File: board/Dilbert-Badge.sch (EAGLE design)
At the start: 47 parts, among them IC1 MCP23017SO, J1 IO EXP., J2 FTDI_DEVICE, J3 NEOPIXEL, J4 PWR IN, J5 I2C, SW1 UP, SW2 DOWN, SW3 LEFT, SW4 RIGHT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

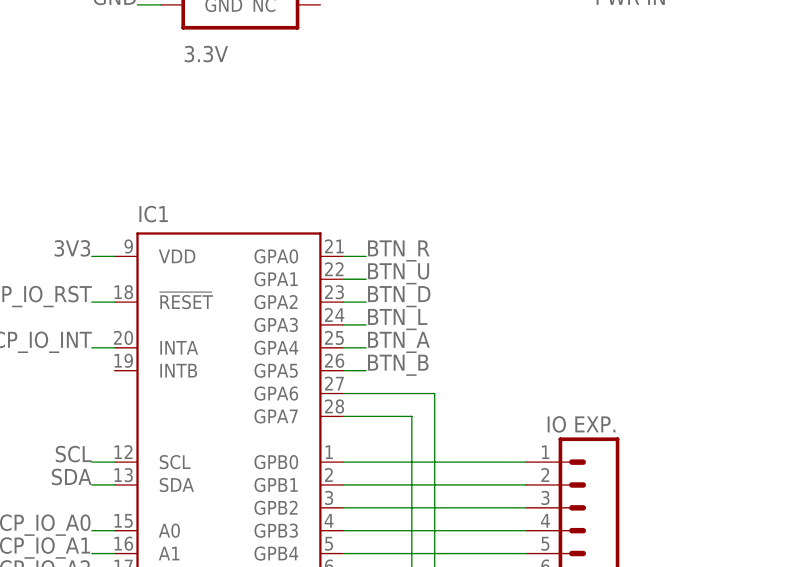
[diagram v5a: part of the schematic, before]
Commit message: swap left/right buttons
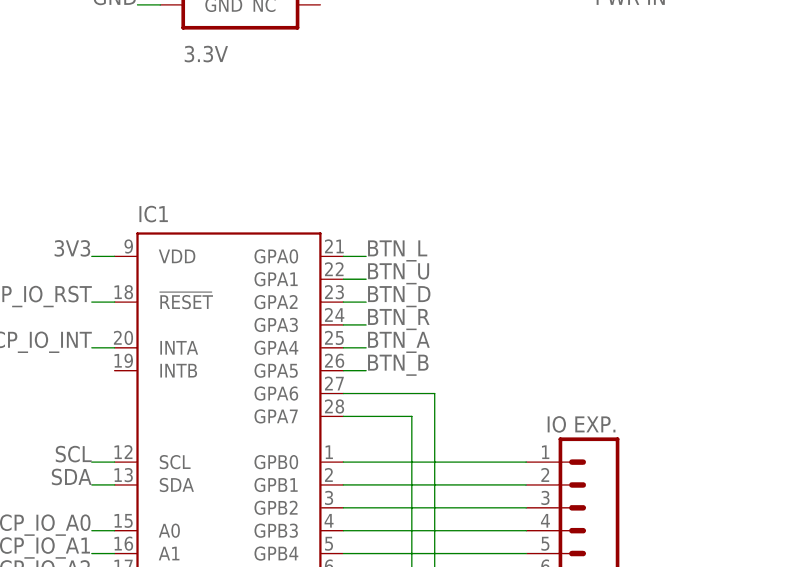
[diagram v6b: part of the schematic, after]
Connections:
- net BTN_L: now also IC1.GPA0; no longer IC1.GPA3
- net BTN_R: now also IC1.GPA3; no longer IC1.GPA0
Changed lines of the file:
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@@
 </segment>
 <segment>
-<pinref part="IC1" gate="G$1" pin="GPA3"/>
-<label x="76.2" y="226.06" size="1.778" layer="95"/>
-<wire x1="76.2" y1="226.06" x2="73.66" y2="226.06" width="0.1524" layer="91"/>
+<pinref part="IC1" gate="G$1" pin="GPA0"/>
+<label x="76.2" y="233.68" size="1.778" layer="95"/>
+<wire x1="73.66" y1="233.68" x2="76.2" y2="233.68" width="0.1524" layer="91"/>
 </segment>
 </net>
@@
 </segment>
 <segment>
-<pinref part="IC1" gate="G$1" pin="GPA0"/>
-<label x="76.2" y="233.68" size="1.778" layer="95"/>
-<wire x1="73.66" y1="233.68" x2="76.2" y2="233.68" width="0.1524" layer="91"/>
+<pinref part="IC1" gate="G$1" pin="GPA3"/>
+<label x="76.2" y="226.06" size="1.778" layer="95"/>
+<wire x1="76.2" y1="226.06" x2="73.66" y2="226.06" width="0.1524" layer="91"/>
 </segment>
 </net>

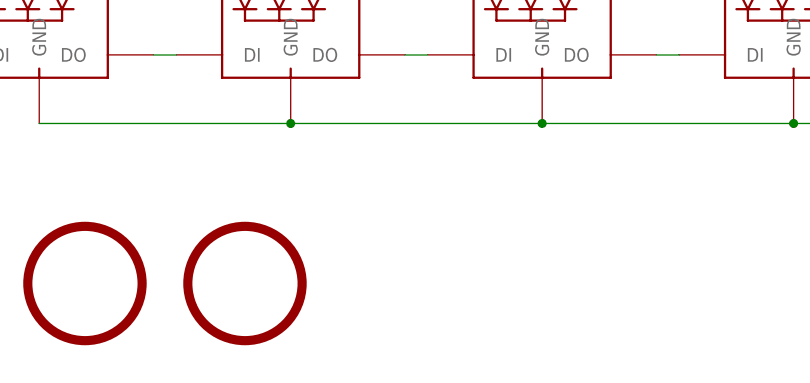
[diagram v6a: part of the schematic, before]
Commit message: Redo Alistair's new layout
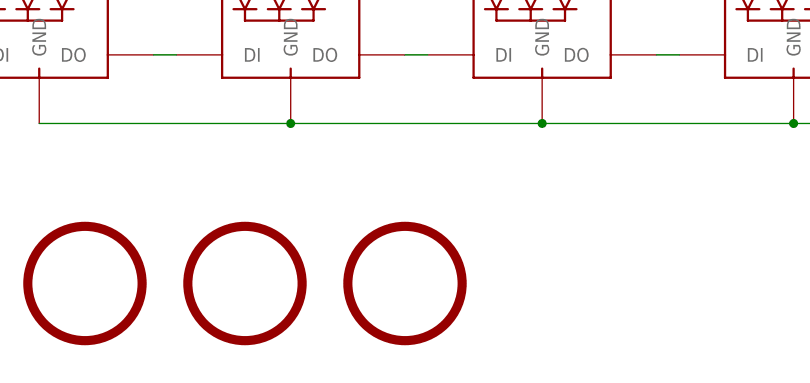
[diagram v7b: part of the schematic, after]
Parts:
- added U$5: 5MM_MOUNTING_HOLE, mechanical:5MM_MOUNTING_HOLE
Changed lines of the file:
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@@
 <part name="C5" library="SparkFun-Capacitors" deviceset="1.0UF-25V-+80/-20(0805)" device="&quot;" value="1.0uF"/>
 <part name="U$4" library="mechanical" deviceset="5MM_MOUNTING_HOLE" device=""/>
+<part name="U$5" library="mechanical" deviceset="5MM_MOUNTING_HOLE" device=""/>
 </parts>
 <sheets>
@@
 <instance part="C5" gate="G$1" x="256.54" y="266.7"/>
 <instance part="U$4" gate="G$1" x="76.2" y="10.16"/>
+<instance part="U$5" gate="G$1" x="93.98" y="10.16"/>
 </instances>
 <busses>
